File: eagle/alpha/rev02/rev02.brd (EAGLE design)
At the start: 100 x 80 mm, 359 parts, among them CN1 HOST, CN2 HOST, IC1 IS45S32160F, IC3 N25Q128A13ES, Q3 2N7002, Q5 ASFL1, Q6 2N7002, T1 BC847, T2 BC847, T3 BC818, U1 MC14551BDG, U2 MC74HC1G14DTT1G, U3 ATTINY828R-AU, U4 MC14551BDG, U5 23K640-I/SN, U6 MCP79412-I/SN, U7 XC7A200TFBG484, Y1 12 MHz, Y2 12 MHz

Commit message: updates after todays call with Pavel
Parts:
- added C190, C191, C192, C202, C203, C209, C210, C211: 0.1uF, resistor:C0402
- added C193, C204, C205: 0.1 uF, resistor:C0402
- added C212: 0.1 uF, resistor:C0603
- added C213: 2.2 uF LowESR, resistor:C0603
- added IC2: IS45S32160F, Alpha-IC:TSOP2-86L
- added IC4: N25Q128A13ES, altera-configdevices:SO08
- added Q1: 2N7002, transistors_gaui:SOT23
- added R73, R74: 4.7k, resistor:R0603
- added R75: 10K, resistor:R0402
- added R76: 1K, resistor:R0402
- JP2: device SparkFun-Connectors:1X03_LOCK -> jumper:JP1
- moved JP2 111.4 mm to (-10.0, -100.0)
- moved C11 71.4 mm to (132.8, 18.0)
- moved C10 71.4 mm to (132.1, 25.9)
- moved C12 71.4 mm to (128.3, 19.6)
- moved C189 71.4 mm to (129.8, 18.0)
- moved FB3 71.4 mm to (127.0, 18.0)
- moved LED17 71.4 mm to (132.6, 20.3)
- moved R69 71.4 mm to (125.5, 19.6)
- moved C181 71.4 mm to (132.6, 22.9)
- moved C183 71.4 mm to (125.2, 20.8)
- moved C184 71.4 mm to (132.6, 28.2)
- moved C185 71.4 mm to (132.6, 19.3)
- moved C188 71.4 mm to (128.0, 20.8)
- moved C9 71.4 mm to (132.3, 24.4)
- moved FB4 71.4 mm to (122.7, 18.5)
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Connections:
- removed net FPGA_ENTROPY_ENABLE: JP2.1
- removed net FPGA_PROM_CS_N: IC3.1, R9.1, U1.2
- removed net VDD: IC1.1
- removed net VDDQ: IC1.3
- new net FMC_SDCKE1: IC2.67, U$1.194
- new net FMC_SDCLK: IC1.68, IC2.68, U$1.135
- new net FMC_SDNE1: IC2.20, U$1.195
- new net FPGA_ENTROPY_DISABLE: R76.1, U7.B18
- new net KSM_PROM_CS_N: IC3.1, IC4.1, R73.2, R9.1, U1.2
- new net KSM_PROM_MISO: IC4.2, U$1.55
- new net KSM_PROM_MOSI: IC4.5, U$1.56
- new net KSM_PROM_SCLK: IC4.6, U$1.54
- new net N$11: Q1.1, R75.1, R76.2
- new net N$14: JP2.2, Q1.3
- net 15V_LDO_ENABLE: now also JP2.1; no longer JP2.2
- net FMC_A0: now also IC2.25
- net FMC_A1: now also IC2.26
- net FMC_A10: now also IC2.24
- net FMC_A11: now also IC2.21
- net FMC_A12: now also IC2.69
- net FMC_A14: now also IC2.22
- net FMC_A15: now also IC2.23
- net FMC_A2: now also IC2.27
- net FMC_A3: now also IC2.60
- net FMC_A4: now also IC2.61
- net FMC_A5: now also IC2.62
- net FMC_A6: now also IC2.63
- net FMC_A7: now also IC2.64
- net FMC_A8: now also IC2.65
- net FMC_A9: now also IC2.66
- net FMC_CLK: no longer IC1.68
- net FMC_D0: now also IC2.2
- net FMC_D1: now also IC2.4
- net FMC_D10: now also IC2.76, IC2.77
- net FMC_D11: now also IC2.79
- net FMC_D12: now also IC2.80
- net FMC_D13: now also IC2.82
- net FMC_D14: now also IC2.83
- net FMC_D15: now also IC2.85
- net FMC_D16: now also IC2.31
- net FMC_D17: now also IC2.33
- net FMC_D18: now also IC2.34
- net FMC_D19: now also IC2.36
- net FMC_D2: now also IC2.5
- net FMC_D20: now also IC2.37
- net FMC_D21: now also IC2.39
- net FMC_D22: now also IC2.40
- net FMC_D23: now also IC2.42
- net FMC_D24: now also IC2.45
- net FMC_D25: now also IC2.47
- net FMC_D26: now also IC2.48
- net FMC_D27: now also IC2.50
- net FMC_D28: now also IC2.51
- net FMC_D29: now also IC2.53
- net FMC_D3: now also IC2.7
- net FMC_D30: now also IC2.54
- net FMC_D31: now also IC2.56
- net FMC_D4: now also IC2.8
- net FMC_D5: now also IC2.10
- net FMC_D6: now also IC2.11
- net FMC_D7: now also IC2.13
- net FMC_D8: now also IC2.74
- net FMC_NBL0: now also IC2.16
- net FMC_NBL1: now also IC2.71
- net FMC_NBL2: now also IC2.28
- net FMC_NBL3: now also IC2.59
- net FMC_SDNCAS: now also IC2.18
- net FMC_SDNRAS: now also IC2.19
- net FMC_SDNWE: now also IC2.17
- net GND: now also C190.2, C191.2, C192.2, C193.2, C202.2, C203.2, C204.2, C205.2, C209.2, C210.2, C211.2, C212.2, C213.2, IC2.12, IC2.32, IC2.38, IC2.44, IC2.46, IC2.52, IC2.58, IC2.6, IC2.72, IC2.78, IC2.84, IC2.86, IC4.4, Q1.2, R73.1, R74.1, R75.2
- net PWR_18V: now also C213.1
- net VCCO_3V3: now also C190.1, C191.1, C192.1, C193.1, C202.1, C203.1, C204.1, C205.1, C209.1, C210.1, C211.1, C212.1, IC1.1, IC1.3, IC2.1, IC2.15, IC2.29, IC2.3, IC2.35, IC2.41, IC2.43, IC2.49, IC2.55, IC2.75, IC2.81, IC4.3, IC4.7, IC4.8, R74.2

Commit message: connect ARM side of SD/MMC, MGMT USB
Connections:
- new net N$23: U$1.143
- new net N$25: U$1.144
- new net N$57: U$1.145
- new net N$58: U$1.146
- new net SDIO_CK: U$1.163
- new net SDIO_CMD: U$1.166
- new net SDIO_D0: U$1.140
- new net SDIO_D1: U$1.141
- new net SDIO_D2: U$1.161
- new net SDIO_D3: U$1.162
- net ARM_FPGA_CFG_CONTROL: now also U$1.118; no longer U$1.166
- net ARM_FPGA_CFG_MISO: now also U$1.106; no longer U$1.162
- net ARM_FPGA_CFG_MOSI: now also U$1.107; no longer U$1.163
- net ARM_FPGA_CFG_SCLK: now also U$1.105; no longer U$1.161
- net FT_CTS: now also U$1.43
- net FT_RTS: now also U$1.44
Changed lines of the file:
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@@
 <setting verticaltext="up"/>
 </settings>
-<grid distance="10" unitdist="mm" unit="mm" style="lines" multiple="1" display="yes" altdistance="25" altunitdist="mil" altunit="mil"/>
+<grid distance="50" unitdist="mil" unit="mil" style="lines" multiple="1" display="yes" altdistance="25" altunitdist="mil" altunit="mil"/>
 <layers>
 <layer number="1" name="Top" color="4" fill="1" visible="yes" active="yes"/>
@@
 <signal name="FT_RTS">
 <contactref element="U$3" pad="15"/>
+<contactref element="U$1" pad="44"/>
+<wire x1="101.5156" y1="12.2148" x2="98.8064" y2="31.138" width="0" layer="19" extent="1-1"/>
 </signal>
 <signal name="FT_CTS">
 <contactref element="U$3" pad="16"/>
+<contactref element="U$1" pad="43"/>
+<wire x1="101.5156" y1="11.7148" x2="98.3238" y2="31.138" width="0" layer="19" extent="1-1"/>
 </signal>
 <signal name="FT_DTR">
@@
 <signal name="ARM_FPGA_CFG_MOSI">
 <contactref element="U1" pad="10"/>
-<contactref element="U$1" pad="163"/>
-<wire x1="75.4892" y1="55.4712" x2="93.6498" y2="84.201" width="0" layer="19" extent="1-1"/>
+<contactref element="U$1" pad="107"/>
+<wire x1="101.829" y1="60.2972" x2="93.6498" y2="84.201" width="0" layer="19" extent="1-1"/>
 </signal>
 <signal name="ARM_FPGA_CFG_MISO">
 <contactref element="U1" pad="1"/>
-<contactref element="U$1" pad="162"/>
-<wire x1="75.4892" y1="55.9792" x2="88.7222" y2="91.821" width="0" layer="19" extent="1-1"/>
+<contactref element="U$1" pad="106"/>
+<wire x1="102.3116" y1="60.2972" x2="88.7222" y2="91.821" width="0" layer="19" extent="1-1"/>
 </signal>
 <signal name="ARM_FPGA_CFG_SCLK">
 <contactref element="U1" pad="12"/>
-<contactref element="U$1" pad="161"/>
-<wire x1="75.4892" y1="56.4618" x2="93.6498" y2="86.741" width="0" layer="19" extent="1-1"/>
+<contactref element="U$1" pad="105"/>
+<wire x1="102.8196" y1="60.2972" x2="93.6498" y2="86.741" width="0" layer="19" extent="1-1"/>
 </signal>
 <signal name="N$3">
@@
 <signal name="ARM_FPGA_CFG_CONTROL">
 <contactref element="JP8" pad="2"/>
-<contactref element="U$1" pad="166"/>
-<wire x1="75.4892" y1="53.9726" x2="96.774" y2="89.408" width="0" layer="19" extent="1-1"/>
+<contactref element="U$1" pad="118"/>
+<wire x1="96.3172" y1="60.2972" x2="96.774" y2="89.408" width="0" layer="19" extent="1-1"/>
 </signal>
 <signal name="FT_RESET1">
@@
 <wire x1="-10.65" y1="-90" x2="59.0808" y2="51.2088" width="0" layer="19" extent="1-1"/>
 </signal>
+<signal name="SDIO_CK">
+<contactref element="U$1" pad="163"/>
+</signal>
+<signal name="SDIO_CMD">
+<contactref element="U$1" pad="166"/>
+</signal>
+<signal name="SDIO_D3">
+<contactref element="U$1" pad="162"/>
+</signal>
+<signal name="SDIO_D2">
+<contactref element="U$1" pad="161"/>
+</signal>
+<signal name="SDIO_D0">
+<contactref element="U$1" pad="140"/>
+</signal>
+<signal name="SDIO_D1">
+<contactref element="U$1" pad="141"/>
+</signal>
+<signal name="N$23">
+<contactref element="U$1" pad="143"/>
+</signal>
+<signal name="N$25">
+<contactref element="U$1" pad="144"/>
+</signal>
+<signal name="N$57">
+<contactref element="U$1" pad="145"/>
+</signal>
+<signal name="N$58">
+<contactref element="U$1" pad="146"/>
+</signal>
 </signals>

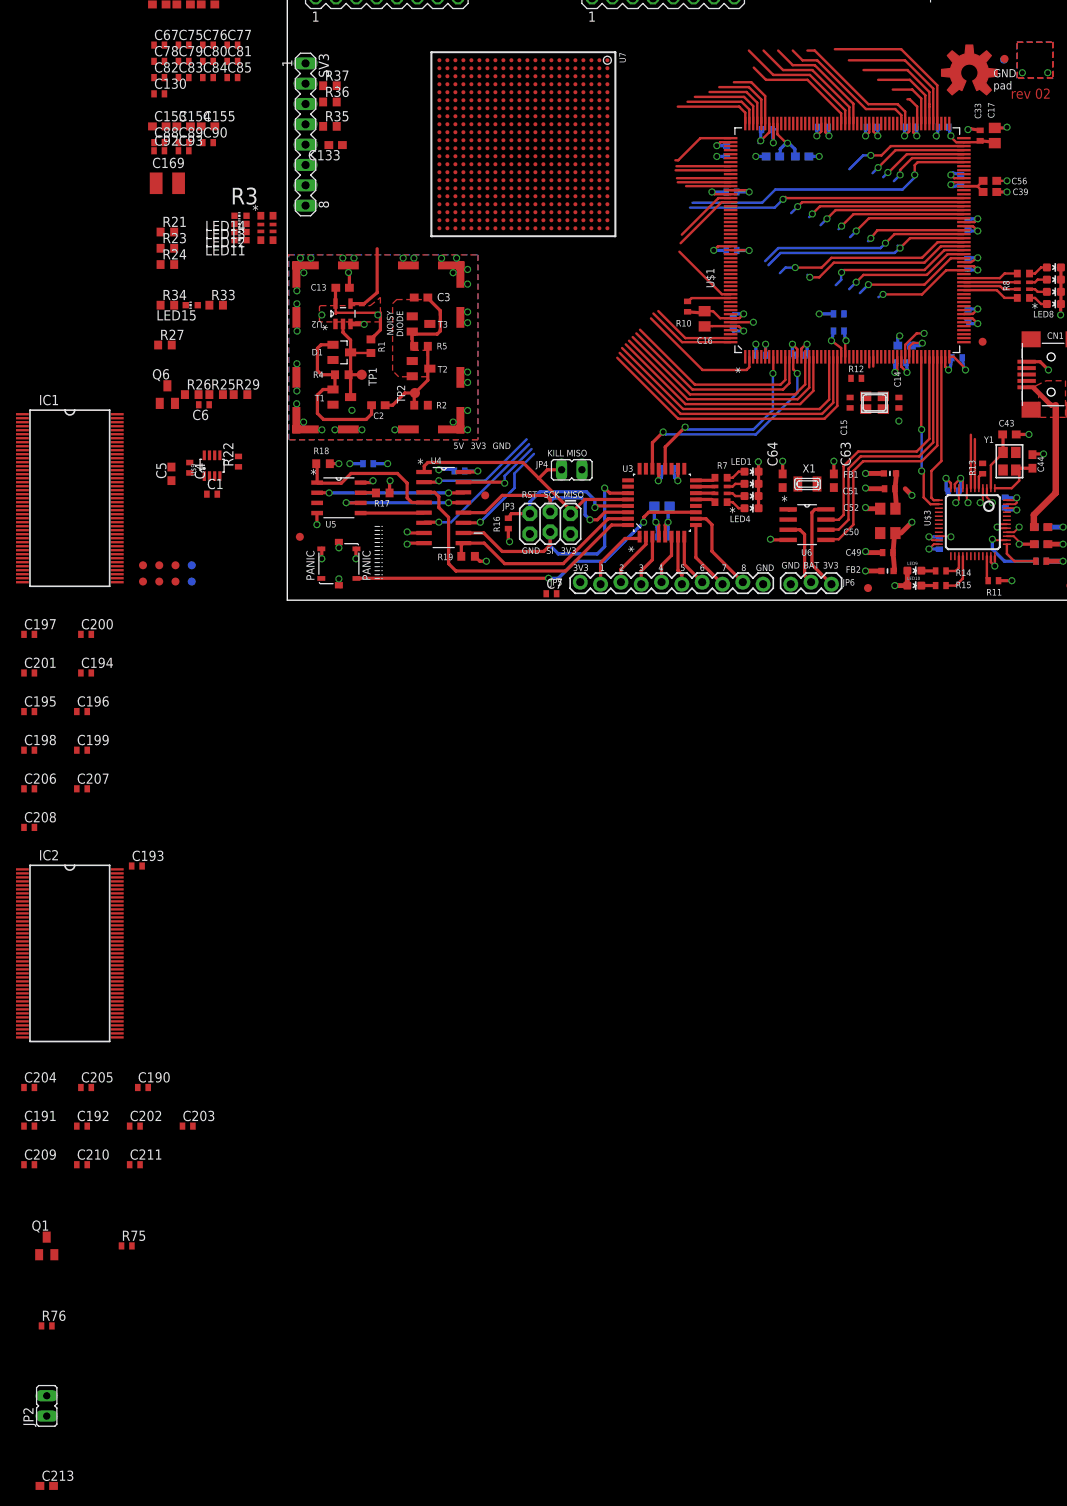
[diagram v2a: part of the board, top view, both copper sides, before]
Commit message: rearrange STM32F429 symbol after functionality instead of hardware
Now that it is more known what functionality we want to use in the STM32,
it makes much more sense (and will help reviewers a great deal) to have
the symbol in the schematics arranged after used functionality rather than
after how the hardware pinout is.
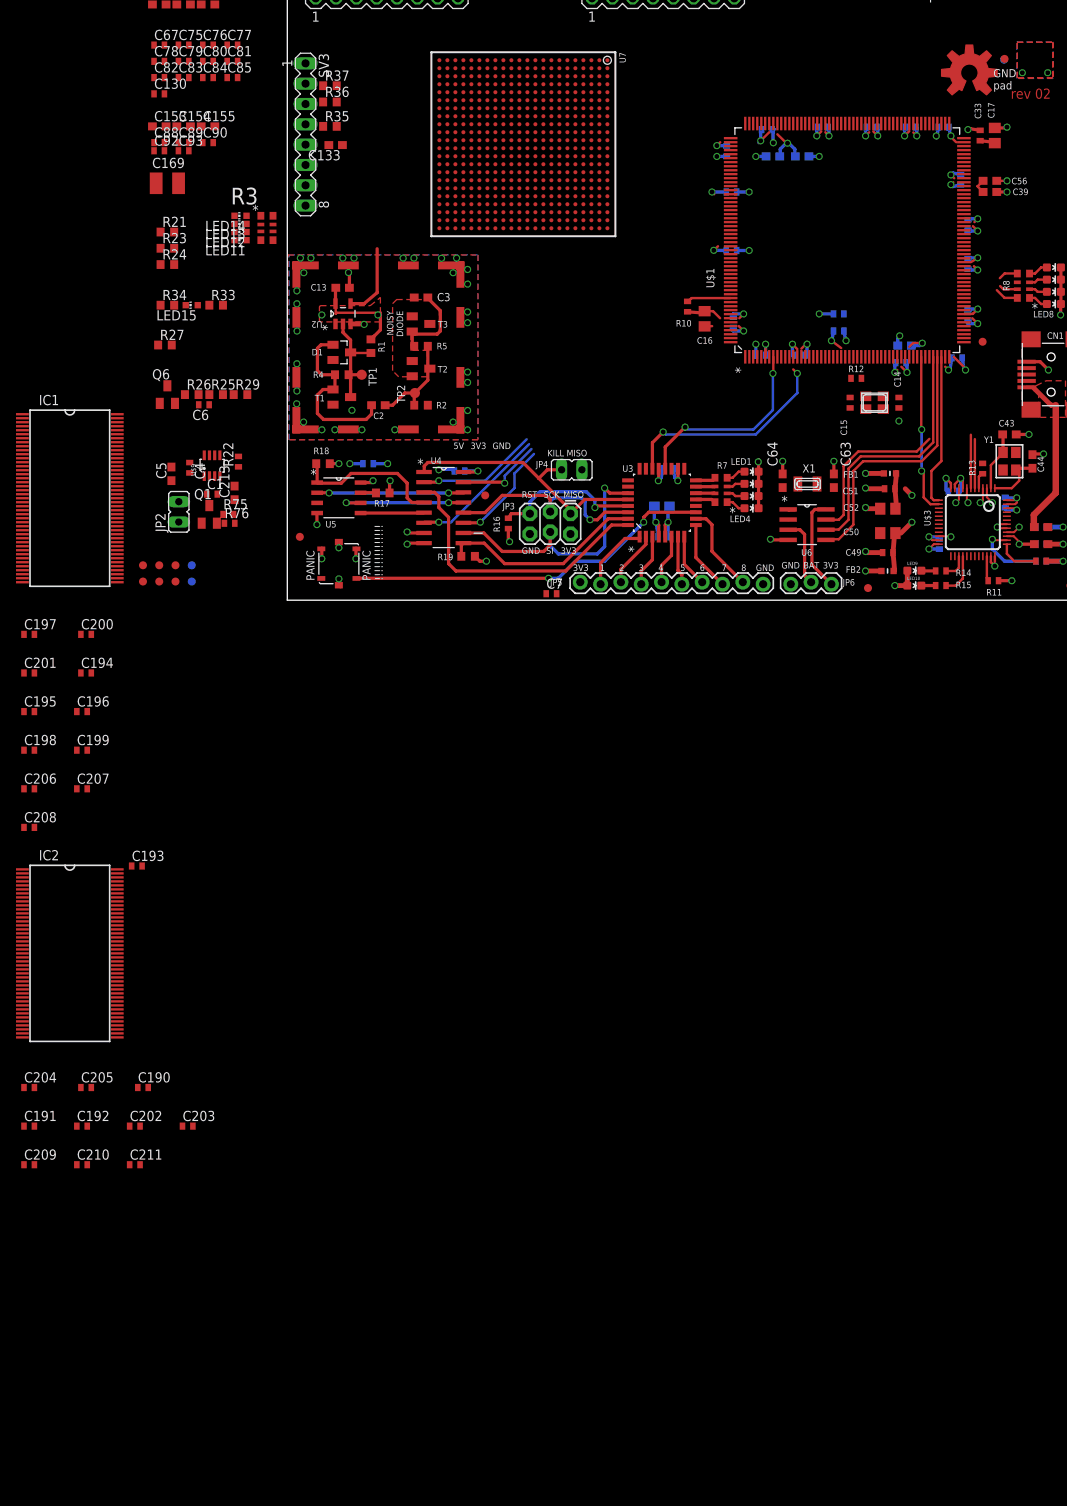
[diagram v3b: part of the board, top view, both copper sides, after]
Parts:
- C38, C39, C56, C57: value 2.2 uF LowESR -> 2.2 uF
- U$1: device STM32F429:LQFP-208 -> Alpha-IC:LQFP-208
- moved C213 126.3 mm to (13.5, 14.1), turned to 90 degrees
- moved JP2 113.0 mm to (6.51, 11.8)
- moved R76 102.9 mm to (12.9, 10.3)
- moved Q1 93.7 mm to (10.3, 11.4)
- moved R75 92.3 mm to (12.7, 11.4)
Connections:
- removed net N$23: U$1.143
- removed net N$25: U$1.144
- removed net N$57: U$1.145
- removed net N$58: U$1.146
- net AVR_GPIO_11: no longer U$1.13
- net FPGA_DONE: now also U$1.119; no longer U$1.36
- net FPGA_IRQ_N_0: now also U$1.175; no longer U$1.181
- net FPGA_IRQ_N_1: now also U$1.174; no longer U$1.180
- net FPGA_IRQ_N_2: now also U$1.123; no longer U$1.179
- net FPGA_IRQ_N_3: now also U$1.122; no longer U$1.178
- net FT_MGMT_CTS: now also U$1.145
- net FT_MGMT_RTS: now also U$1.146
- net FT_MGMT_RXD: now also U$1.143
- net FT_MGMT_TXD: now also U$1.144
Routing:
- net FMC_A5: track 37.5 -> 0.00 mm
- net FMC_D16: track 36.9 -> 0.00 mm, vias 1 -> 0
- net FMC_A4: track 36.2 -> 0.00 mm
- net FMC_D12: track 35.2 -> 0.00 mm, vias 1 -> 0
- net FMC_A3: track 34.9 -> 0.00 mm
- net VCCO_3V3: track 113.6 -> 79.1 mm, vias 27 -> 25
- net FMC_A2: track 31.5 -> 0.00 mm
- net FMC_A1: track 30.0 -> 0.00 mm
- net FMC_A0: track 28.5 -> 0.00 mm
- net FMC_D4: track 26.3 -> 0.00 mm, vias 1 -> 0
- net FMC_D5: track 26.3 -> 0.00 mm, vias 1 -> 0
- net FMC_D31: track 25.7 -> 0.00 mm
- net FMC_A11: track 24.6 -> 0.00 mm, vias 1 -> 0
- net FMC_D30: track 24.1 -> 0.00 mm
- net FMC_D11: track 22.5 -> 0.00 mm, vias 1 -> 0
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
